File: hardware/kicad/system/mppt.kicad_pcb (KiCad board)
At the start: 2 copper layers, 165 x 82 mm, 21 parts, among them J1 PV ind, J2 til lager (V3), J3 sense -> Arduino, Q1 TIP41A, U1 LM358

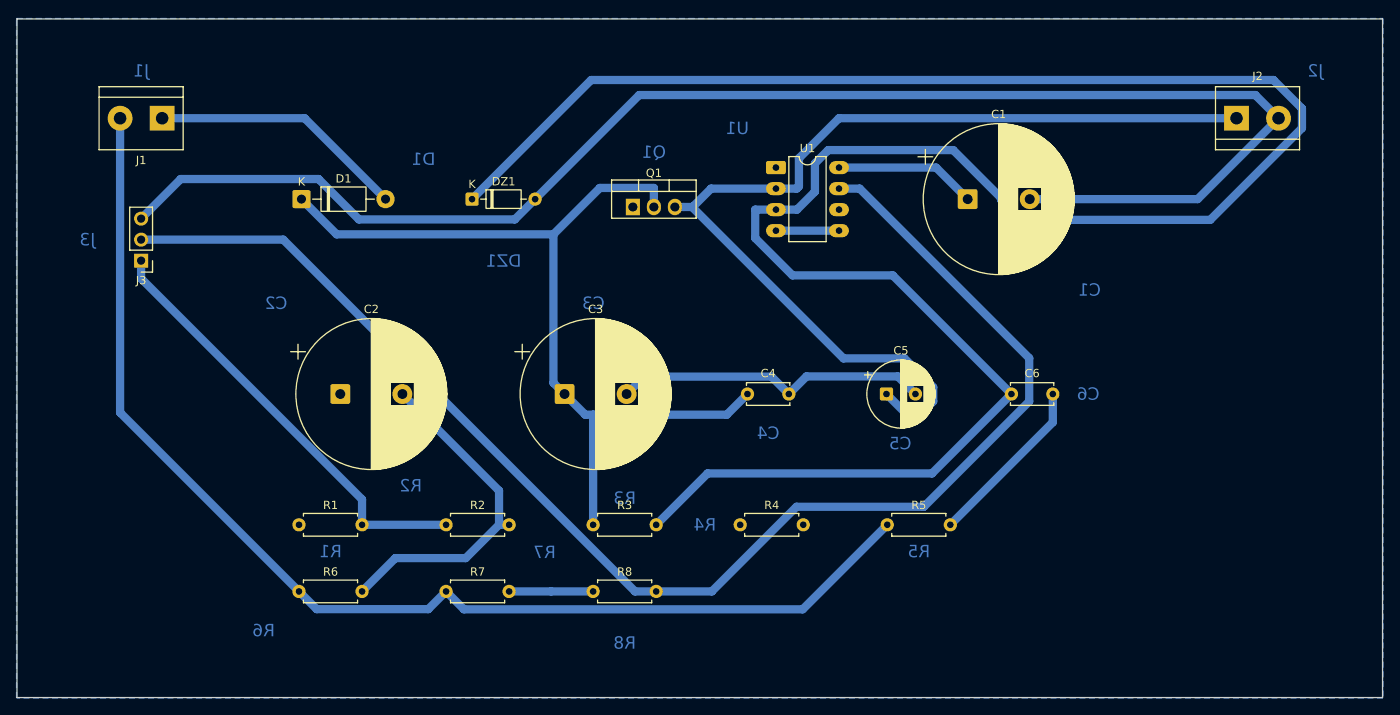
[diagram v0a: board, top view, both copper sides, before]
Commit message: Hand-place mppt and current_sense following the signal flow
The auto-grid placement scattered the per-channel parts and starved the
single-layer router: current_sense had 15 airwires (a third of the
board hand-wired) and mppt 10. pcb_build.py now takes an explicit
placement table for these two - channels run left to right (terminal ->
shunt -> gain pair -> op-amp -> header), PV chain likewise - and the
boards shrank in the process (mppt 165x82 -> 140x68, current_sense
134x58 -> 120x80).

Jumpers now: mppt 7, current_sense 10, both DRC-clean (one cosmetic
silk-over-mask warning on mppt; silk isn't part of the laser flow).
Also fixed in this pass: shunt pair R5/R6 flipped so same-net pads
face each other, and a local 'import json' that shadowed the module
import and broke pcb_build entirely. Production DXF/gerbers re-exported,
cut sizes and jumper tables updated.
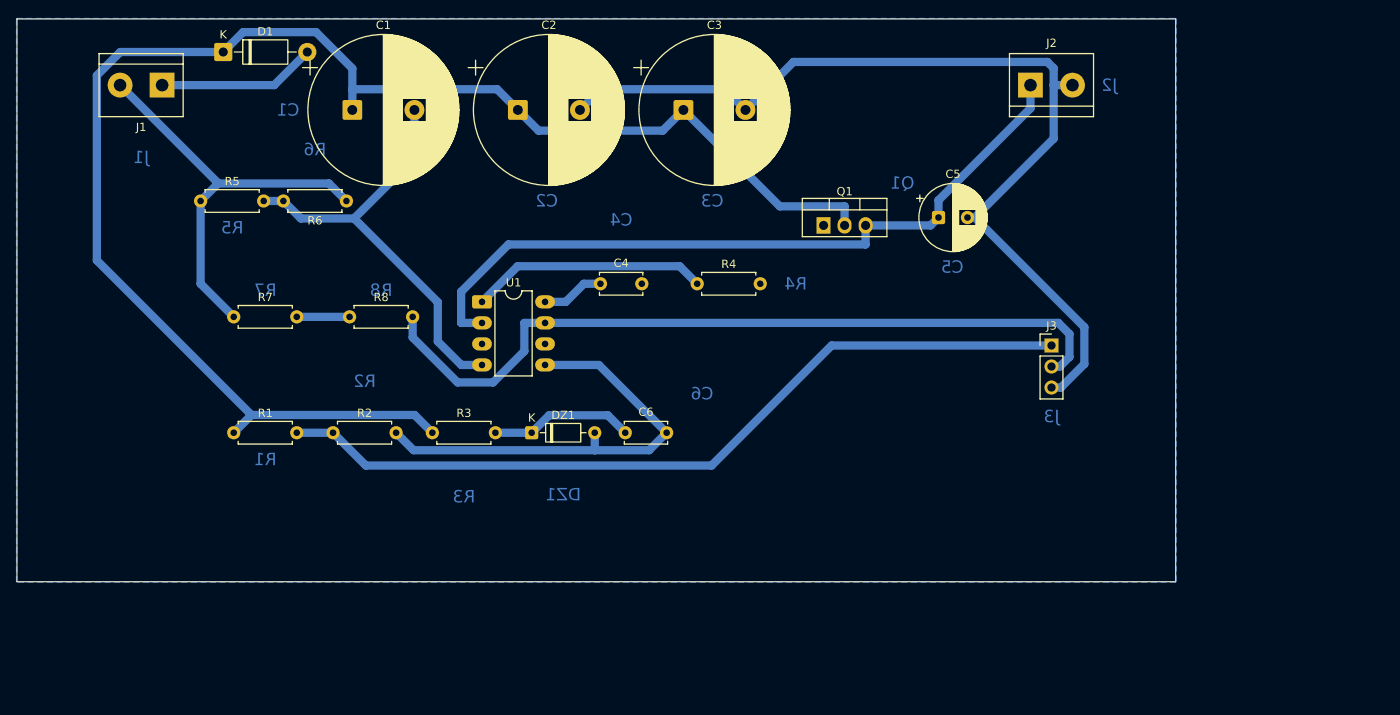
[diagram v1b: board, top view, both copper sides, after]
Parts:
- moved J3 110.5 mm to (145.0, 59.5), turned to 0 degrees
- moved R5 91.7 mm to (42.2, 42.0)
- moved C1 75.1 mm to (60.5, 31.0)
- moved R6 47.5 mm to (59.8, 42.0), turned to 180 degrees
- moved C6 46.9 mm to (93.5, 70.0)
- moved R8 44.3 mm to (60.2, 56.0)
- moved R7 41.9 mm to (46.2, 56.0)
- moved C2 40.5 mm to (80.5, 31.0)
- moved U1 39.0 mm to (76.2, 54.2)
- moved C3 37.2 mm to (100.5, 31.0)
- moved R4 29.6 mm to (102.2, 52.0)
- moved DZ1 29.1 mm to (82.2, 70.0)
- moved J2 25.2 mm to (142.5, 28.0)
- moved Q1 23.2 mm to (117.5, 45.0)
- moved R3 22.4 mm to (70.2, 70.0)
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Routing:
- net /VREF: track 281.0 -> 17.4 mm
- net /PV_RET: track 144.1 -> 51.8 mm
- net /PV_I: track 171.1 -> 95.0 mm
- net /PV_BUS: track 123.4 -> 191.7 mm
- net GND: track 291.6 -> 223.6 mm
- net /PV_V: track 53.1 -> 98.8 mm
- net /V3_OUT: track 121.2 -> 89.6 mm
- net /U1A_OUT: track 0.00 -> 28.7 mm
- net /PV_PLUS: track 31.0 -> 19.2 mm
- net /U1B_FB: track 10.1 -> 6.38 mm
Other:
- board size 165 x 82 mm -> 140 x 68 mm
- board text removed: "D1"
- board text removed: "U1"
